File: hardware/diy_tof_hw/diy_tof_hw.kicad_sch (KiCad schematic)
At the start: 0 parts

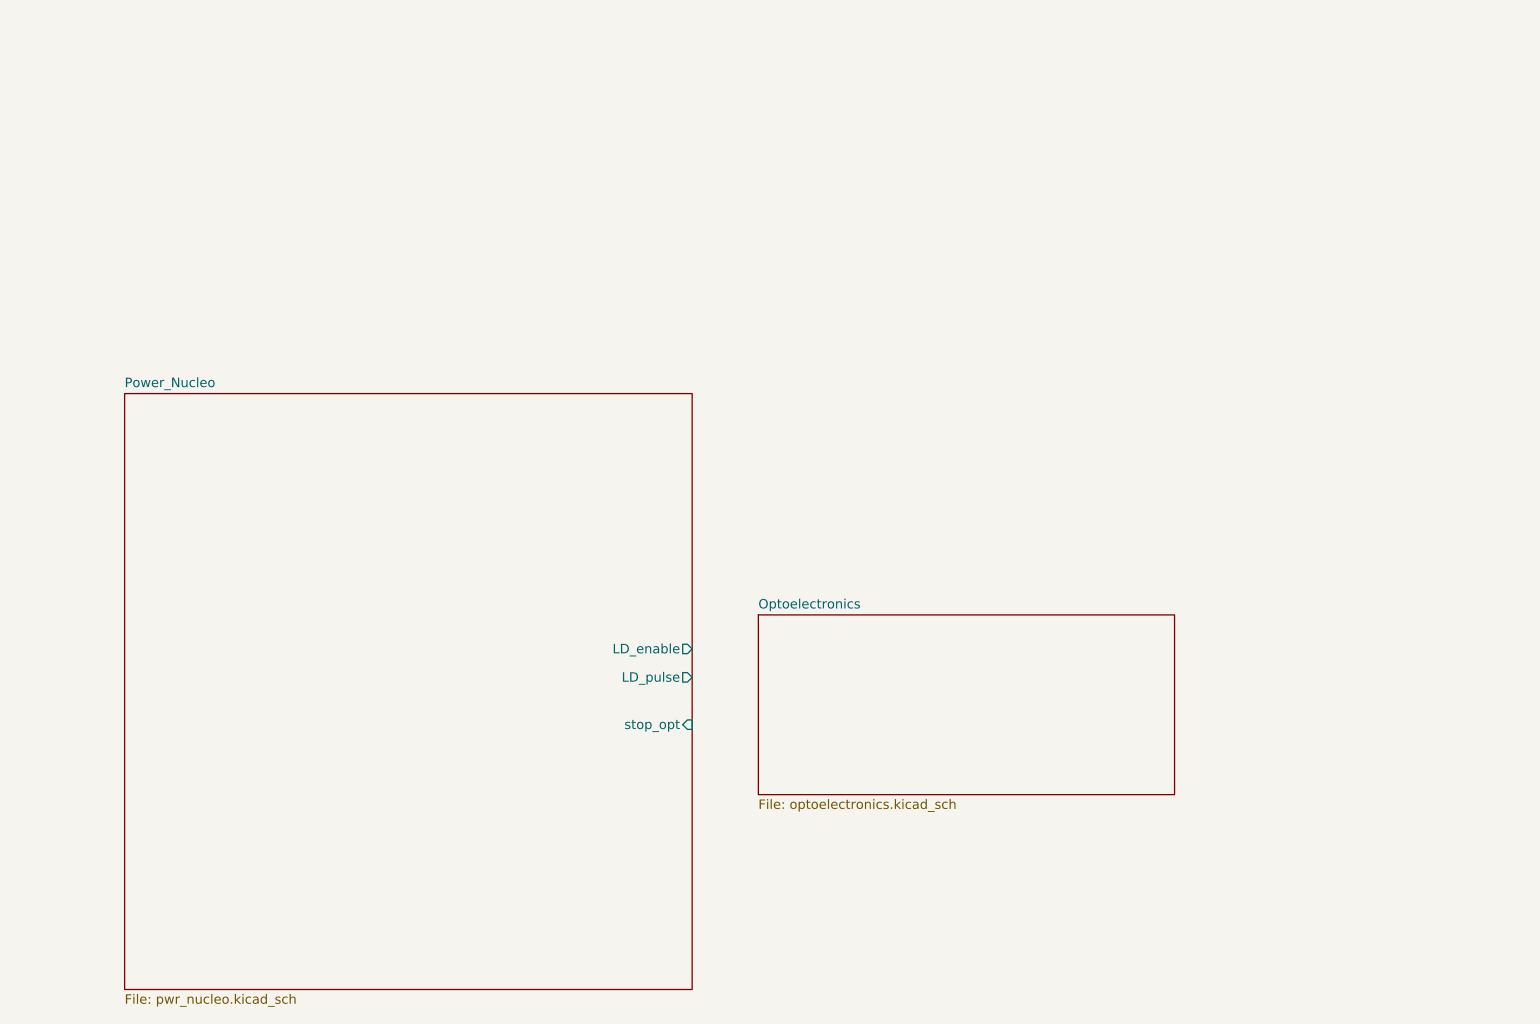
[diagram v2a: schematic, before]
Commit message: [hardware] added schematics and library components for the laser driver as well as TIA circuit
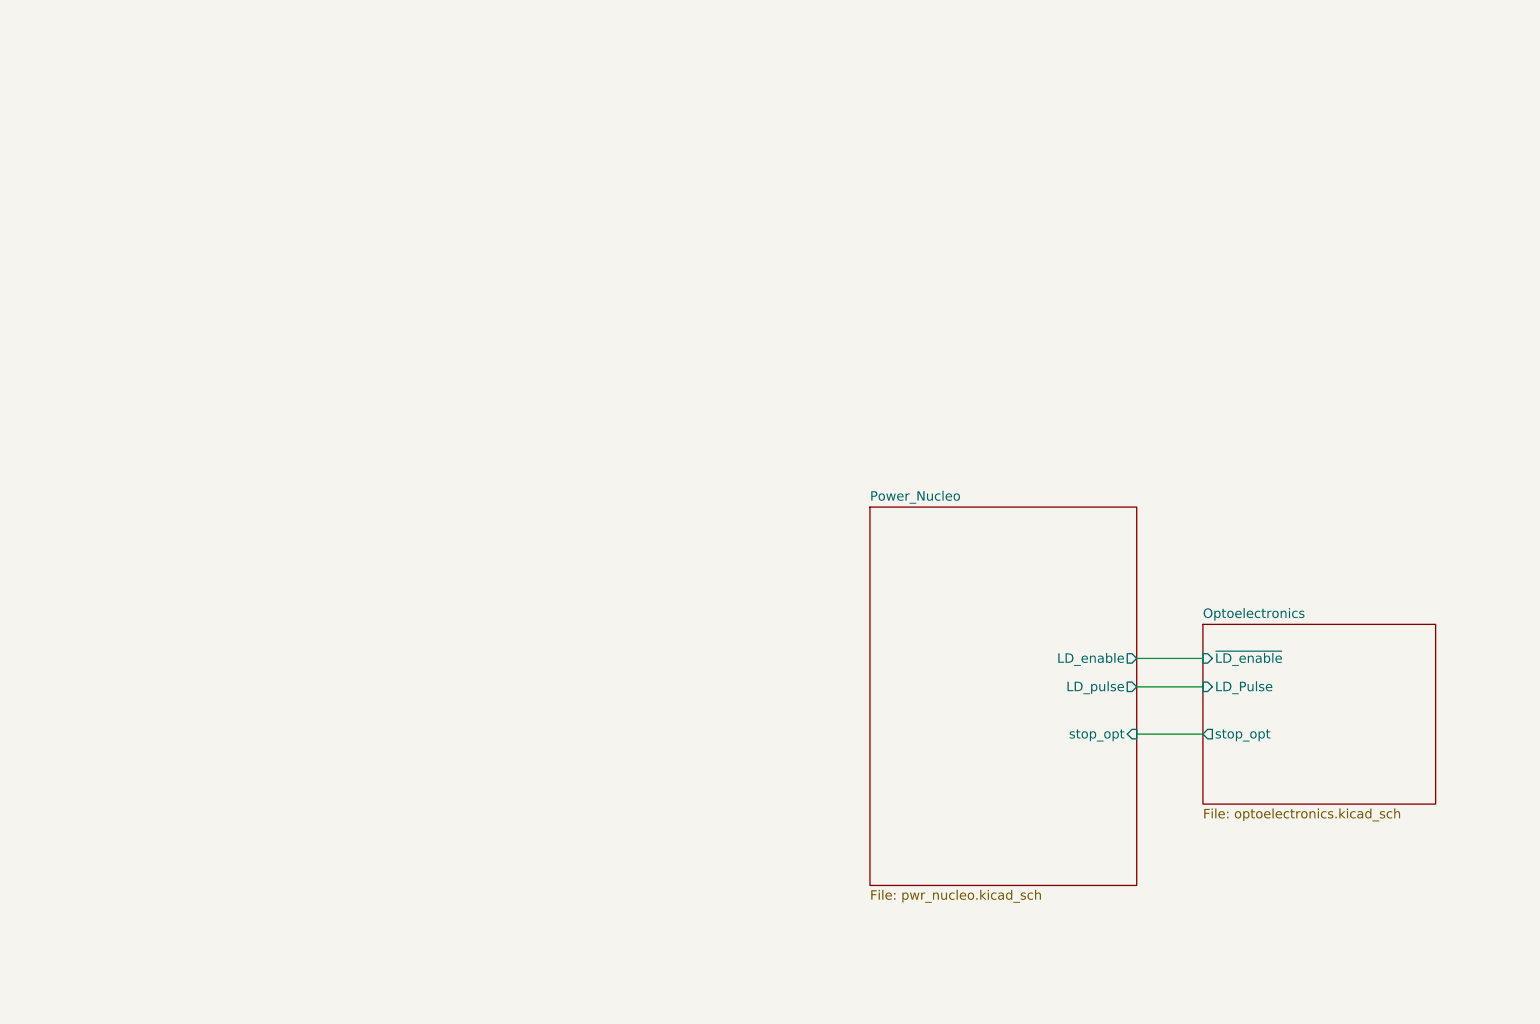
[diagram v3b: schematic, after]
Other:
- sheet Optoelectronics ports: added LD_Pulse, stop_opt, ~{LD_enable}; removed none
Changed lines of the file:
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@@
 		(comment 8 "M. Schär")
 	)
+	(wire
+		(pts
+			(xy 196.85 125.73) (xy 205.74 125.73)
+		)
+		(stroke
+			(width 0)
+			(type default)
+		)
+	)
+	(wire
+		(pts
+			(xy 196.85 115.57) (xy 205.74 115.57)
+		)
+		(stroke
+			(width 0)
+			(type default)
+		)
+	)
+	(wire
+		(pts
+			(xy 196.85 119.38) (xy 205.74 119.38)
+		)
+		(stroke
+			(width 0)
+			(type default)
+		)
+	)
 	(sheet
-		(at 146.05 109.728)
-		(size 55.88 24.13)
+		(at 205.74 110.998)
+		(size 31.242 24.13)
 		(fields_autoplaced yes)
 		(stroke
@@
 		)
 		(property "Sheetname" "Optoelectronics"
-			(at 146.05 109.0164 0)
+			(at 205.74 110.2864 0)
 			(effects
 				(font
@@
 		)
 		(property "Sheetfile" "optoelectronics.kicad_sch"
-			(at 146.05 134.4426 0)
+			(at 205.74 135.7126 0)
 			(effects
 				(font
@@
 				)
 				(justify left top)
+			)
+		)
+		(pin "~{LD_enable}" input
+			(at 205.74 115.57 180)
+			(effects
+				(font
+					(size 1.27 1.27)
+				)
+				(justify left)
+			)
+		)
+		(pin "LD_Pulse" input
+			(at 205.74 119.38 180)
+			(effects
+				(font
+					(size 1.27 1.27)
+				)
+				(justify left)
+			)
+		)
+		(pin "stop_opt" output
+			(at 205.74 125.73 180)
+			(effects
+				(font
+					(size 1.27 1.27)
+				)
+				(justify left)
 			)
 		)
@@
 	)
 	(sheet
-		(at 60.96 80.01)
-		(size 76.2 80.01)
+		(at 161.036 95.25)
+		(size 35.814 50.8)
 		(fields_autoplaced yes)
 		(stroke
@@
 		)
 		(property "Sheetname" "Power_Nucleo"
-			(at 60.96 79.2984 0)
+			(at 161.036 94.5384 0)
 			(effects
 				(font
@@
 		)
 		(property "Sheetfile" "pwr_nucleo.kicad_sch"
-			(at 60.96 160.6046 0)
+			(at 161.036 146.6346 0)
 			(effects
 				(font
@@
 		)
 		(pin "LD_pulse" output
-			(at 137.16 118.11 0)
+			(at 196.85 119.38 0)
 			(effects
 				(font
@@
 		)
 		(pin "stop_opt" input
-			(at 137.16 124.46 0)
+			(at 196.85 125.73 0)
 			(effects
 				(font
@@
 		)
 		(pin "LD_enable" output
-			(at 137.16 114.3 0)
+			(at 196.85 115.57 0)
 			(effects
 				(font

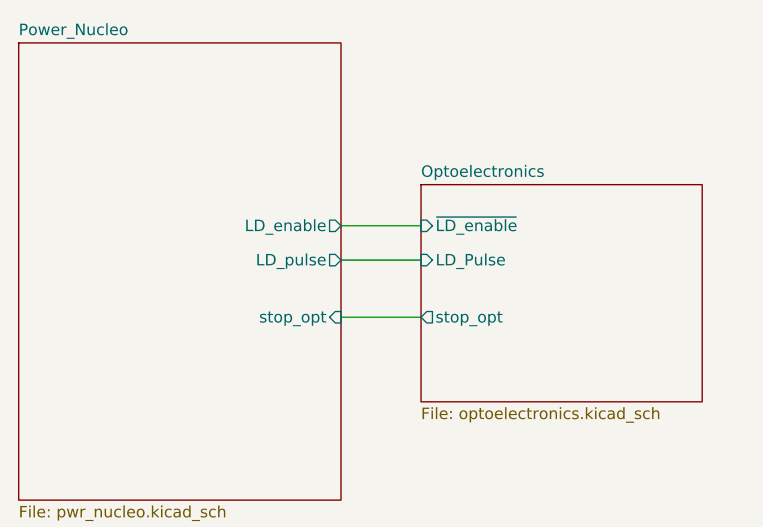
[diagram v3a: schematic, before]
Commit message: [hardware, firmware] various review findings  - added new signals TDC_opt/ele_enable  - fixed placement and appearance of the optics mount  - added switch for stop signal of the electrical TDC  - replaced "ground bead" with a 0R (in order to have a single clamping point for GND)  - added some additional decoupling caps for the laser driver  - reversed polarisation of the PD  - added a small resistor in between TIA and comparator  - adjusted RC to have higher capacitance and lower resistance  - cleaned up some labels / port names
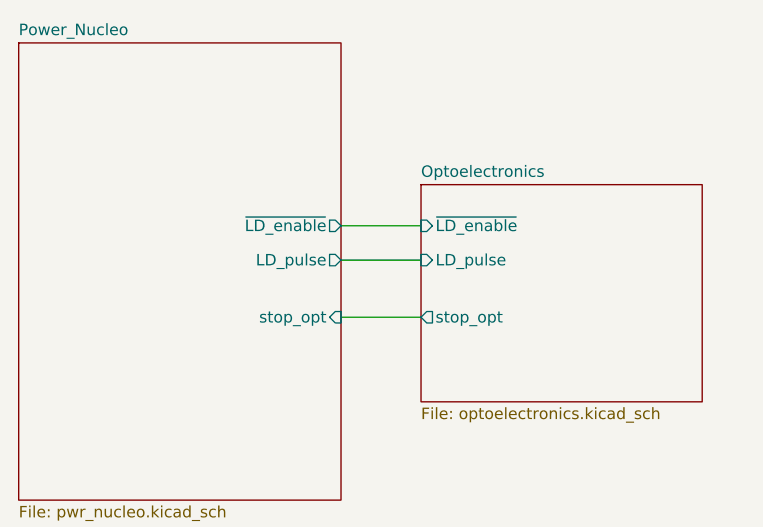
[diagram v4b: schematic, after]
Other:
- sheet Optoelectronics ports: added LD_pulse; removed LD_Pulse
- sheet Power_Nucleo ports: added ~{LD_enable}; removed LD_enable
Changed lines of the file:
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@@
 			)
 		)
-		(pin "LD_Pulse" input
-			(at 205.74 119.38 180)
+		(pin "stop_opt" output
+			(at 205.74 125.73 180)
 			(effects
 				(font
@@
 			)
 		)
-		(pin "stop_opt" output
-			(at 205.74 125.73 180)
+		(pin "LD_pulse" input
+			(at 205.74 119.38 180)
 			(effects
 				(font
@@
 			)
 		)
-		(pin "LD_enable" output
+		(pin "~{LD_enable}" output
 			(at 196.85 115.57 0)
 			(effects

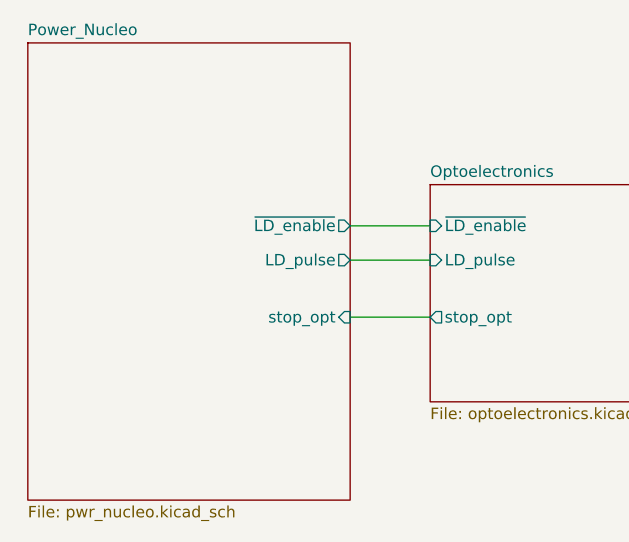
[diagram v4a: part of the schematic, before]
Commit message: [hardware] renamed sheet "pwr_nucleo" to "pwr_nucleo_tdc"
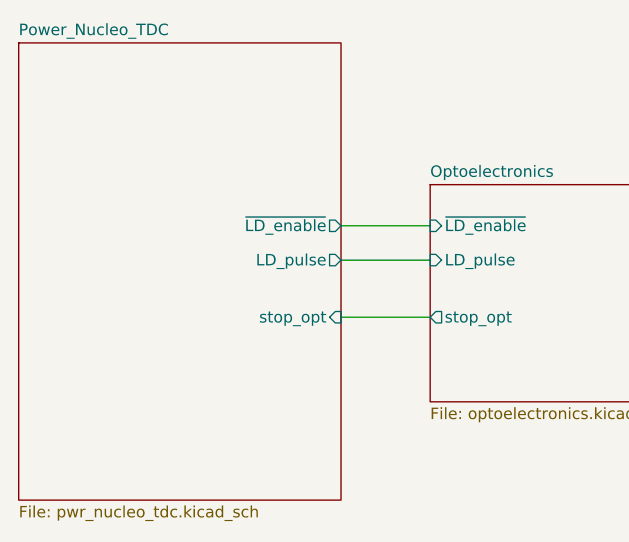
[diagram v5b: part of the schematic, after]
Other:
- sheet Power_Nucleo renamed Power_Nucleo_TDC
- sheet Power_Nucleo_TDC: file pwr_nucleo.kicad_sch -> pwr_nucleo_tdc.kicad_sch
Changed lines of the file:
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@@
 	(wire
 		(pts
-			(xy 196.85 125.73) (xy 205.74 125.73)
+			(xy 195.834 119.38) (xy 205.74 119.38)
 		)
 		(stroke
@@
 	(wire
 		(pts
-			(xy 196.85 115.57) (xy 205.74 115.57)
+			(xy 195.834 125.73) (xy 205.74 125.73)
 		)
 		(stroke
@@
 	(wire
 		(pts
-			(xy 196.85 119.38) (xy 205.74 119.38)
+			(xy 195.834 115.57) (xy 205.74 115.57)
 		)
 		(stroke
@@
 	)
 	(sheet
-		(at 161.036 95.25)
+		(at 160.02 95.25)
 		(size 35.814 50.8)
 		(fields_autoplaced yes)
@@
 			(color 0 0 0 0.0000)
 		)
-		(property "Sheetname" "Power_Nucleo"
-			(at 161.036 94.5384 0)
+		(property "Sheetname" "Power_Nucleo_TDC"
+			(at 160.02 94.5384 0)
 			(effects
 				(font
@@
 			)
 		)
-		(property "Sheetfile" "pwr_nucleo.kicad_sch"
-			(at 161.036 146.6346 0)
+		(property "Sheetfile" "pwr_nucleo_tdc.kicad_sch"
+			(at 160.02 146.6346 0)
 			(effects
 				(font
@@
 		)
 		(pin "LD_pulse" output
-			(at 196.85 119.38 0)
+			(at 195.834 119.38 0)
 			(effects
 				(font
@@
 		)
 		(pin "stop_opt" input
-			(at 196.85 125.73 0)
+			(at 195.834 125.73 0)
 			(effects
 				(font
@@
 		)
 		(pin "~{LD_enable}" output
-			(at 196.85 115.57 0)
+			(at 195.834 115.57 0)
 			(effects
 				(font
